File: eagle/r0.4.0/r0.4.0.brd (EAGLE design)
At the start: 56.8 x 43.2 mm, 8 parts

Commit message: Added finishing touches to r0.4.0 of the board
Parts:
- removed JP1: (no value), pinhead:2X02
- added USB: value?, pinhead:2X02
- moved 12VDC_AND_LED 1.80 mm to (45.7, 21.6)
- moved Y_TILT 1.27 mm to (10.2, 16.5)
- moved C1 1.27 mm to (5.08, 21.6)
- moved RF_HEADER 1.27 mm to (8.89, 29.2)
- moved RF_HEADER1 1.27 mm to (29.2, 20.3)
- moved U$1 1.27 mm to (27.9, 20.3)
- moved X_TILT 1.27 mm to (41.9, 36.8)
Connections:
- new net N$4: 12VDC_AND_LED.B1, 12VDC_AND_LED.B6, RF_HEADER1.1, RF_HEADER1.3, RF_HEADER1.5, RF_HEADER1.7, U$1.4, USB.1, X_TILT.2
- new net N$7: 12VDC_AND_LED.B5, U$1.8
- net N$11: now also 12VDC_AND_LED.B4, U$1.9; no longer 12VDC_AND_LED.B1, 12VDC_AND_LED.B6, JP1.2, RF_HEADER1.1, RF_HEADER1.3, RF_HEADER1.5, RF_HEADER1.7, U$1.4, X_TILT.2
- net N$9: now also USB.3; no longer JP1.4
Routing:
- net N$4: track 0.00 -> 96.8 mm, vias 0 -> 2
- net N$11: track 71.5 -> 19.1 mm
- net N$2: track 0.00 -> 32.2 mm
- net N$7: track 0.00 -> 12.7 mm
- net N$3: track 0.00 -> 7.62 mm
- net N$5: track 0.00 -> 5.08 mm
- net N$22: track 0.00 -> 5.08 mm
- net N$13: track 0.00 -> 5.08 mm
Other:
- board size 56.8 x 43.2 mm -> 57.5 x 44.4 mm
- board text added: "0 di ck V V 0"
- board text added: "0v"
- board text added: "5v"
- board text removed: "v ck cs g g v"

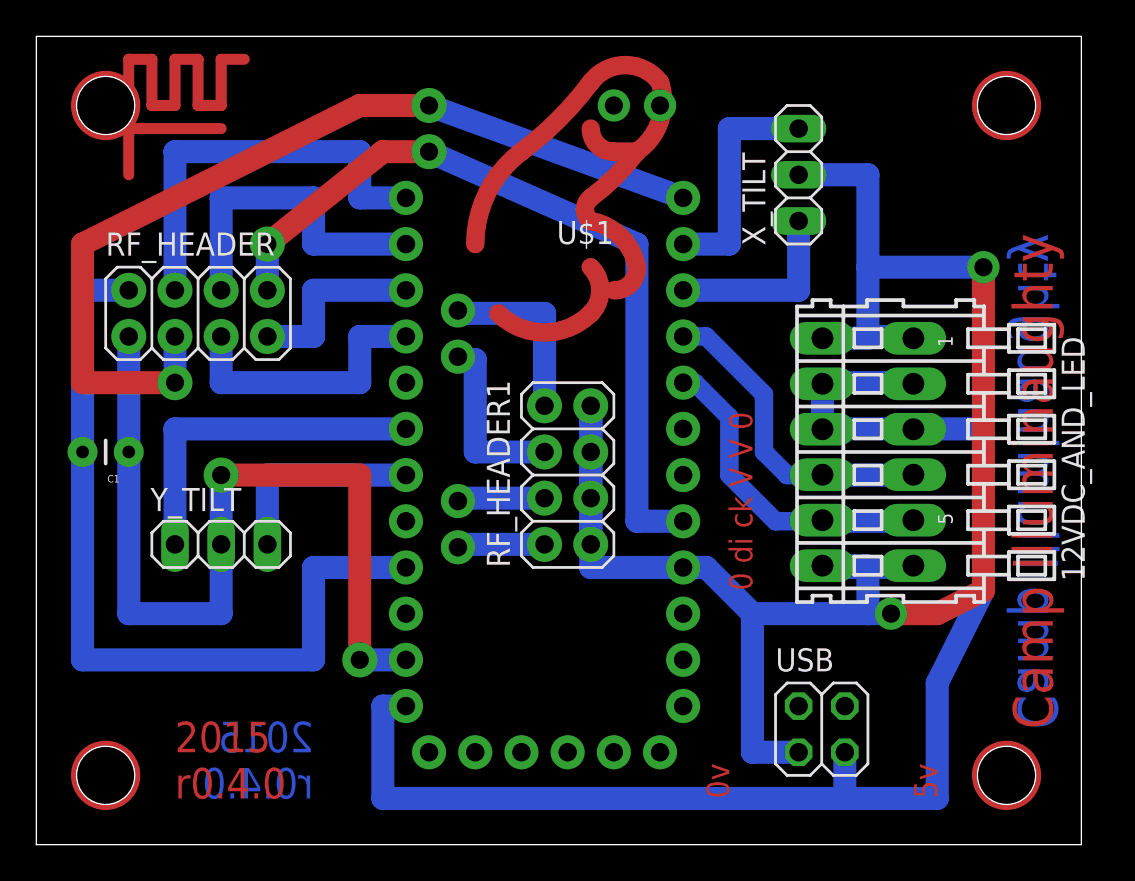
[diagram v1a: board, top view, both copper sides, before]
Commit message: Updated r0.4.0 of the board: * Thickened usb header pads * Added a couple of pads for unused pins
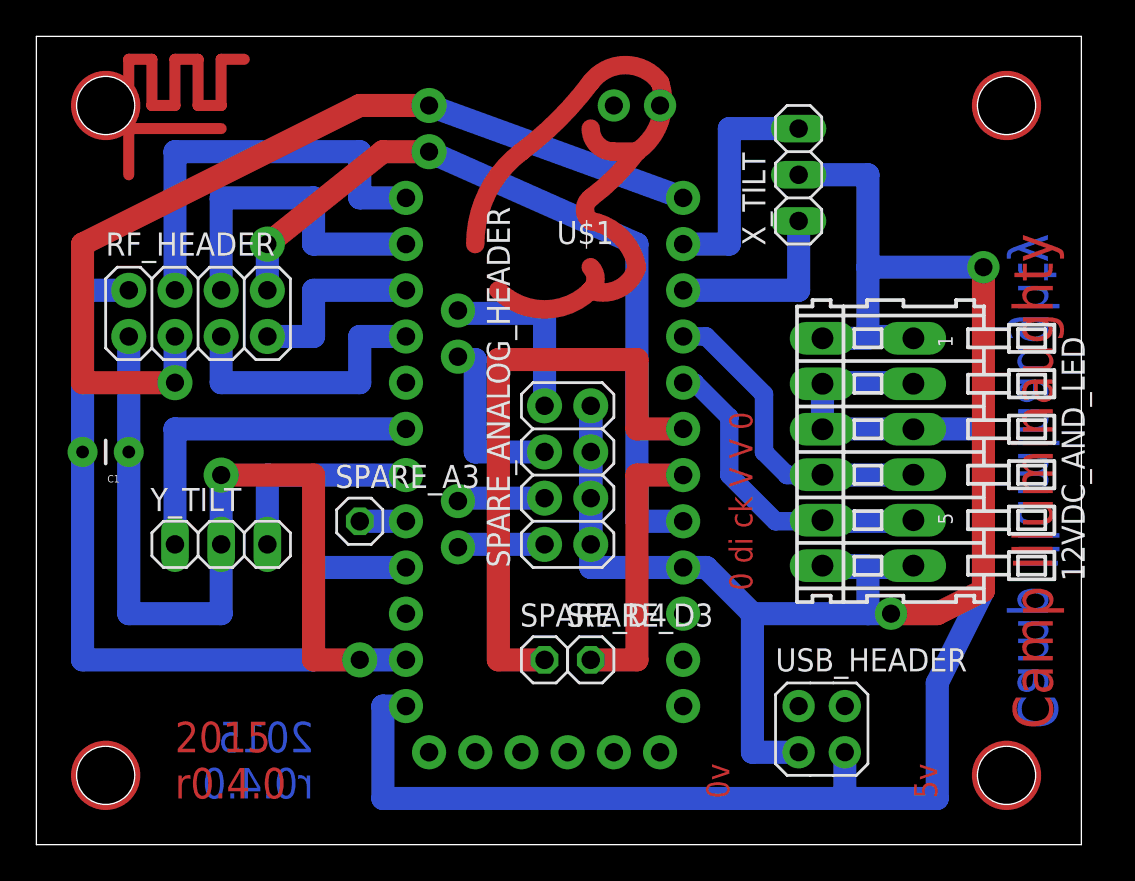
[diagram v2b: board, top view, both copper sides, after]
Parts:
- removed USB: value?, pinhead:2X02
- added SPARE_A3, SPARE_D3, SPARE_D4: (no value), pinhead:1X01
- added USB_HEADER: (no value), usb-header:2X02
- renumbered RF_HEADER1 to SPARE_ANALOG_HEADER
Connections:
- new net N$28: SPARE_A3.1, U$1.20
- new net N$29: SPARE_D3.1, U$1.6
- new net N$30: SPARE_D4.1, U$1.7
- net N$4: now also USB_HEADER.1; no longer USB.1
- net N$9: now also USB_HEADER.3; no longer USB.3
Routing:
- net N$30: track 0.00 -> 33.0 mm
- net N$29: track 0.00 -> 15.2 mm
- net N$28: track 0.00 -> 2.54 mm
- net N$3: track 7.62 -> 6.35 mm
- net N$2: track 32.2 -> 33.3 mm
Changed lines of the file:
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@@
 <element name="C1" library="SparkFun-Passives" package="CAP-PTH-SMALL" value="10u" x="5.08" y="21.59" rot="R180"/>
 <element name="RF_HEADER" library="rf-header" package="2X04" value="value?" x="8.89" y="29.21"/>
-<element name="RF_HEADER1" library="rf-header" package="2X04" value="value?" x="29.21" y="20.32" rot="R90"/>
+<element name="SPARE_ANALOG_HEADER" library="rf-header" package="2X04" value="value?" x="29.21" y="20.32" rot="R90"/>
 <element name="12VDC_AND_LED" library="con-wago" package="234-206" value="value?" x="45.72" y="21.59" rot="R270">
 <attribute name="OC_NEWARK" value="28K9095" x="45.72" y="21.59" size="1.778" layer="27" rot="R270" display="off"/>
@@
 <attribute name="OC_FARNELL" value="unknown" x="45.72" y="21.59" size="1.778" layer="27" rot="R270" display="off"/>
 </element>
-<element name="USB" library="pinhead" package="2X02" value="value?" x="43.18" y="6.35"/>
+<element name="SPARE_A3" library="pinhead" package="1X01" value="" x="17.78" y="17.78"/>
+<element name="SPARE_D3" library="pinhead" package="1X01" value="" x="30.48" y="10.16"/>
+<element name="SPARE_D4" library="pinhead" package="1X01" value="" x="27.94" y="10.16"/>
+<element name="USB_HEADER" library="usb-header" package="2X02" value="" x="43.18" y="6.35"/>
 </elements>
 <signals>
@@
 <wire x1="52.07" y1="13.97" x2="52.07" y2="22.86" width="1.27" layer="16"/>
 <wire x1="52.07" y1="22.86" x2="43.22" y2="22.86" width="1.27" layer="16"/>
-<contactref element="USB" pad="3"/>
+<contactref element="USB_HEADER" pad="3"/>
 <wire x1="44.45" y1="5.08" x2="44.45" y2="2.54" width="1.27" layer="16"/>
 </signal>
@@
 <wire x1="10.16" y1="16.51" x2="10.16" y2="20.32" width="1.27" layer="16"/>
 <via x="10.16" y="20.32" extent="1-16" drill="1" diameter="1.9304"/>
-<wire x1="10.16" y1="20.32" x2="17.78" y2="20.32" width="1.27" layer="1"/>
-<wire x1="17.78" y1="20.32" x2="17.78" y2="10.16" width="1.27" layer="1"/>
 <via x="17.78" y="10.16" extent="1-16" drill="1" diameter="1.9304"/>
 <wire x1="17.78" y1="10.16" x2="20.32" y2="10.16" width="1.27" layer="16"/>
+<wire x1="17.78" y1="10.16" x2="15.24" y2="10.16" width="1.27" layer="1"/>
+<wire x1="15.24" y1="10.16" x2="15.24" y2="20.32" width="1.27" layer="1"/>
+<wire x1="15.24" y1="20.32" x2="10.16" y2="20.32" width="1.27" layer="1"/>
 </signal>
 <signal name="N$12">
 <contactref element="U$1" pad="A4"/>
-<contactref element="RF_HEADER1" pad="4"/>
+<contactref element="SPARE_ANALOG_HEADER" pad="4"/>
 <wire x1="27.94" y1="19.05" x2="23.33625" y2="19.05" width="1.27" layer="16"/>
 <wire x1="23.33625" y1="19.05" x2="23.1775" y2="18.89125" width="1.27" layer="16"/>
@@
 <signal name="N$18">
 <contactref element="U$1" pad="A5"/>
-<contactref element="RF_HEADER1" pad="2"/>
+<contactref element="SPARE_ANALOG_HEADER" pad="2"/>
 <wire x1="27.94" y1="16.51" x2="23.33625" y2="16.51" width="1.27" layer="16"/>
 <wire x1="23.33625" y1="16.51" x2="23.1775" y2="16.35125" width="1.27" layer="16"/>
@@
 <signal name="N$19">
 <contactref element="U$1" pad="A6"/>
-<contactref element="RF_HEADER1" pad="8"/>
+<contactref element="SPARE_ANALOG_HEADER" pad="8"/>
 <wire x1="27.94" y1="24.13" x2="27.94" y2="29.21" width="1.27" layer="16"/>
 <wire x1="27.94" y1="29.21" x2="23.33625" y2="29.21" width="1.27" layer="16"/>
@@
 <signal name="N$20">
 <contactref element="U$1" pad="A7"/>
-<contactref element="RF_HEADER1" pad="6"/>
+<contactref element="SPARE_ANALOG_HEADER" pad="6"/>
 <wire x1="27.94" y1="21.59" x2="24.13" y2="21.59" width="1.27" layer="16"/>
 <wire x1="24.13" y1="21.59" x2="24.13" y2="26.67" width="1.27" layer="16"/>
@@
 <wire x1="30.48" y1="35.56" x2="30.48" y2="34.29" width="1.016" layer="1" curve="106.260205"/>
 <wire x1="30.48" y1="34.29" x2="33.02" y2="31.75" width="1.016" layer="1" curve="-69.390693"/>
-<wire x1="33.02" y1="31.75" x2="31.75" y2="30.48" width="1.016" layer="1" curve="-94.349096"/>
+<wire x1="33.02" y1="31.75" x2="30.48" y2="30.48" width="1.016" layer="1" curve="-94.349096"/>
 <wire x1="33.02" y1="38.1" x2="31.75" y2="38.1" width="1.016" layer="1"/>
 <wire x1="31.75" y1="38.1" x2="30.48" y2="39.37" width="1.016" layer="1" curve="-90"/>
 </signal>
 <signal name="N$3">
-<wire x1="30.48" y1="31.75" x2="30.48" y2="29.21" width="1.016" layer="1" curve="-90"/>
-<wire x1="30.48" y1="29.21" x2="25.4" y2="29.21" width="1.016" layer="1" curve="-90"/>
+<wire x1="30.48" y1="31.75" x2="30.48" y2="30.48" width="1.016" layer="1" curve="-90"/>
+<wire x1="30.48" y1="30.48" x2="25.4" y2="30.48" width="1.016" layer="1" curve="-90"/>
 </signal>
 <signal name="N$4">
-<contactref element="RF_HEADER1" pad="7"/>
-<contactref element="RF_HEADER1" pad="5"/>
+<contactref element="SPARE_ANALOG_HEADER" pad="7"/>
+<contactref element="SPARE_ANALOG_HEADER" pad="5"/>
 <contactref element="X_TILT" pad="2"/>
-<contactref element="RF_HEADER1" pad="1"/>
+<contactref element="SPARE_ANALOG_HEADER" pad="1"/>
 <contactref element="12VDC_AND_LED" pad="B6"/>
 <contactref element="12VDC_AND_LED" pad="B1"/>
 <contactref element="U$1" pad="4"/>
-<contactref element="RF_HEADER1" pad="3"/>
+<contactref element="SPARE_ANALOG_HEADER" pad="3"/>
 <wire x1="43.22" y1="15.34" x2="43.18" y2="15.34" width="1.27" layer="16"/>
 <wire x1="35.56" y1="15.24" x2="30.48" y2="15.24" width="1.27" layer="16"/>
@@
 <wire x1="41.91" y1="36.83" x2="45.72" y2="36.83" width="1.27" layer="16"/>
 <wire x1="45.72" y1="36.83" x2="45.72" y2="31.75" width="1.27" layer="16"/>
-<contactref element="USB" pad="1"/>
 <wire x1="39.37" y1="12.7" x2="39.37" y2="5.08" width="1.27" layer="16"/>
-<wire x1="39.37" y1="5.08" x2="41.91" y2="5.08" width="1.27" layer="16"/>
 <wire x1="39.37" y1="12.7" x2="45.72" y2="12.7" width="1.27" layer="16"/>
 <wire x1="45.72" y1="12.7" x2="46.99" y2="12.7" width="1.27" layer="16"/>
@@
 <wire x1="45.62" y1="15.34" x2="45.72" y2="15.24" width="1.27" layer="16"/>
 <wire x1="45.72" y1="15.24" x2="45.72" y2="12.7" width="1.27" layer="16"/>
+<contactref element="USB_HEADER" pad="1"/>
+<wire x1="41.91" y1="5.08" x2="39.37" y2="5.08" width="1.27" layer="16"/>
 </signal>
 <signal name="N$7">
@@
 <via x="34.29" y="40.64" extent="1-16" drill="1" diameter="1.778"/>
 </signal>
+<signal name="N$28">
+<contactref element="SPARE_A3" pad="1"/>
+<contactref element="U$1" pad="20"/>
+<wire x1="20.32" y1="17.78" x2="17.78" y2="17.78" width="1.27" layer="16"/>
+</signal>
+<signal name="N$29">
+<contactref element="SPARE_D3" pad="1"/>
+<contactref element="U$1" pad="6"/>
+<wire x1="30.48" y1="10.16" x2="33.02" y2="10.16" width="1.27" layer="1"/>
+<wire x1="33.02" y1="10.16" x2="33.02" y2="20.32" width="1.27" layer="1"/>
+<wire x1="33.02" y1="20.32" x2="35.56" y2="20.32" width="1.27" layer="1"/>
+</signal>
+<signal name="N$30">
+<contactref element="SPARE_D4" pad="1"/>
+<contactref element="U$1" pad="7"/>
+<wire x1="35.56" y1="22.86" x2="33.02" y2="22.86" width="1.27" layer="1"/>
+<wire x1="33.02" y1="22.86" x2="33.02" y2="26.67" width="1.27" layer="1"/>
+<wire x1="33.02" y1="26.67" x2="25.4" y2="26.67" width="1.27" layer="1"/>
+<wire x1="25.4" y1="26.67" x2="25.4" y2="10.16" width="1.27" layer="1"/>
+<wire x1="25.4" y1="10.16" x2="27.94" y2="10.16" width="1.27" layer="1"/>
+</signal>
 </signals>
